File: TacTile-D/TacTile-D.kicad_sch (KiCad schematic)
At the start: 12 parts, among them J18 Conn_01x04, J18 Conn_01x06, J19 Conn_01x05, J19 Conn_01x06, J20 Conn_01x02, J20 Conn_01x06, J21 Conn_01x02, J21 Conn_01x06, U12 74HC595, U13 74HC590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

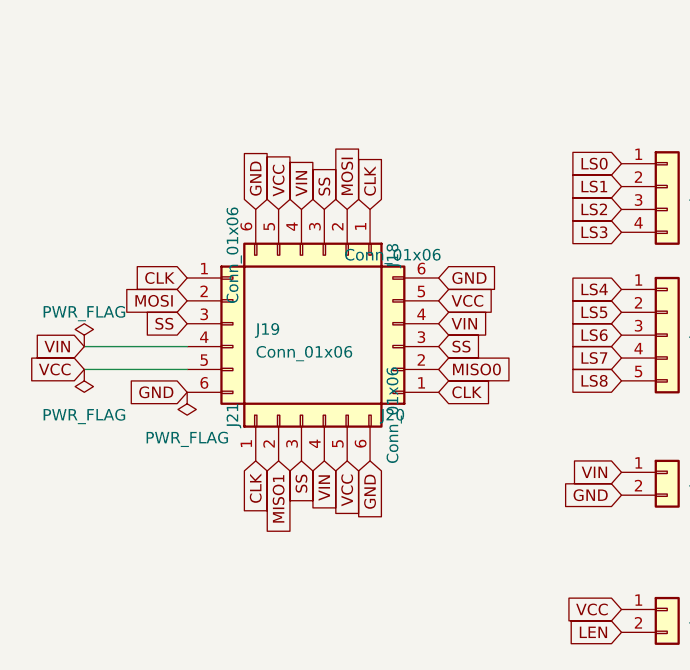
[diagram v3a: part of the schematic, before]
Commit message: Enlarged connectors on board D to 2.54mm pitch
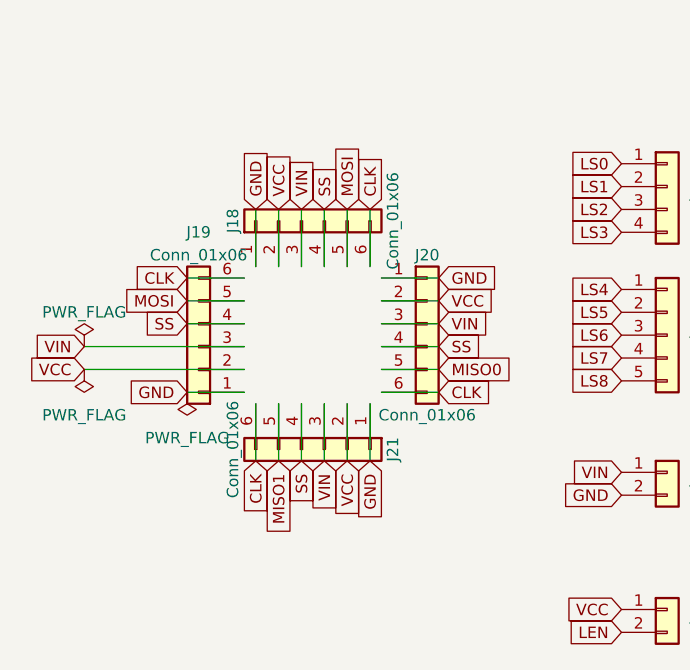
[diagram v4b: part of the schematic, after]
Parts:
- J18, J19: footprint Connector_PinHeader_2.00mm:PinHeader_1x06_P2.00mm_Horizontal -> Connector_PinSocket_2.54mm:PinSocket_1x06_P2.54mm_Horizontal
- J18: footprint Connector_PinSocket_1.27mm:PinSocket_1x04_P1.27mm_Vertical -> Connector_PinSocket_2.54mm:PinSocket_1x04_P2.54mm_Vertical
- J19: footprint Connector_PinSocket_1.27mm:PinSocket_1x05_P1.27mm_Vertical -> Connector_PinSocket_2.54mm:PinSocket_1x05_P2.54mm_Vertical
- J20, J21: footprint Connector_PinSocket_2.00mm:PinSocket_1x06_P2.00mm_Horizontal -> Connector_PinHeader_2.54mm:PinHeader_1x06_P2.54mm_Horizontal
- J20, J21: footprint Connector_PinSocket_1.27mm:PinSocket_1x02_P1.27mm_Vertical -> Connector_PinSocket_2.54mm:PinSocket_1x02_P2.54mm_Vertical
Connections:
- net CLK: now also J18.6 (Pin_6), J19.6 (Pin_6), J20.6 (Pin_6), J21.6 (Pin_6); no longer J18.1 (Pin_1), J19.1 (Pin_1), J20.1 (Pin_1), J21.1 (Pin_1)
- net GND: now also J18.1 (Pin_1), J19.1 (Pin_1), J20.1 (Pin_1), J21.1 (Pin_1); no longer J18.6 (Pin_6), J19.6 (Pin_6), J20.6 (Pin_6), J21.6 (Pin_6)
- net MISO0: now also J20.5 (Pin_5); no longer J20.2 (Pin_2)
- net MISO1: now also J21.5 (Pin_5); no longer J21.2 (Pin_2)
- net MOSI: now also J18.5 (Pin_5), J19.5 (Pin_5); no longer J18.2 (Pin_2), J19.2 (Pin_2)
- net SS: now also J18.4 (Pin_4), J19.4 (Pin_4), J20.4 (Pin_4), J21.4 (Pin_4); no longer J18.3 (Pin_3), J19.3 (Pin_3), J20.3 (Pin_3), J21.3 (Pin_3)
- net VCC: now also J18.2 (Pin_2), J19.2 (Pin_2), J20.2 (Pin_2), J21.2 (Pin_2); no longer J18.5 (Pin_5), J19.5 (Pin_5), J20.5 (Pin_5), J21.5 (Pin_5)
- net VIN: now also J18.3 (Pin_3), J19.3 (Pin_3), J20.3 (Pin_3), J21.3 (Pin_3); no longer J18.4 (Pin_4), J19.4 (Pin_4), J20.4 (Pin_4), J21.4 (Pin_4)
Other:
- moved on the sheet: J18, J19, J20, J21
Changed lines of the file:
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@@
+    (stroke (width 0) (type default))
+  )
+  (wire (pts (xy 46.99 21.59) (xy 46.99 27.94))
+    (stroke (width 0) (type default))
+  )
+  (wire (pts (xy 49.53 43.18) (xy 49.53 49.53))
     (stroke (width 0) (type default))
   )
@@
     (stroke (width 0) (type default))
   )
+  (wire (pts (xy 41.91 43.18) (xy 41.91 49.53))
+    (stroke (width 0) (type default))
+  )
+  (wire (pts (xy 53.34 39.37) (xy 59.69 39.37))
+    (stroke (width 0) (type default))
+  )
+  (wire (pts (xy 39.37 21.59) (xy 39.37 27.94))
+    (stroke (width 0) (type default))
+  )
   (wire (pts (xy 59.69 83.82) (xy 44.45 83.82))
     (stroke (width 0) (type default))
@@
     (stroke (width 0) (type default))
   )
+  (wire (pts (xy 44.45 21.59) (xy 44.45 27.94))
+    (stroke (width 0) (type default))
+  )
   (wire (pts (xy 129.54 128.27) (xy 129.54 91.44))
     (stroke (width 0) (type default))
   )
+  (wire (pts (xy 31.75 34.29) (xy 38.1 34.29))
+    (stroke (width 0) (type default))
+  )
   (wire (pts (xy 123.19 88.9) (xy 129.54 88.9))
     (stroke (width 0) (type default))
   )
+  (wire (pts (xy 53.34 34.29) (xy 59.69 34.29))
+    (stroke (width 0) (type default))
+  )
+  (wire (pts (xy 31.75 41.91) (xy 38.1 41.91))
+    (stroke (width 0) (type default))
+  )
   (wire (pts (xy 67.31 91.44) (xy 59.69 91.44))
     (stroke (width 0) (type default))
@@
     (stroke (width 0) (type default))
   )
+  (wire (pts (xy 31.75 31.75) (xy 38.1 31.75))
+    (stroke (width 0) (type default))
+  )
   (wire (pts (xy 67.31 96.52) (xy 67.31 95.25))
     (stroke (width 0) (type default))
@@
     (stroke (width 0) (type default))
   )
+  (wire (pts (xy 31.75 29.21) (xy 38.1 29.21))
+    (stroke (width 0) (type default))
+  )
+  (wire (pts (xy 20.32 39.37) (xy 38.1 39.37))
+    (stroke (width 0) (type default))
+  )
+  (wire (pts (xy 52.07 21.59) (xy 52.07 27.94))
+    (stroke (width 0) (type default))
+  )
   (wire (pts (xy 95.25 90.17) (xy 95.25 91.44))
     (stroke (width 0) (type default))
@@
     (stroke (width 0) (type default))
   )
-  (wire (pts (xy 20.32 39.37) (xy 31.75 39.37))
+  (wire (pts (xy 46.99 43.18) (xy 46.99 49.53))
+    (stroke (width 0) (type default))
+  )
+  (wire (pts (xy 41.91 21.59) (xy 41.91 27.94))
+    (stroke (width 0) (type default))
+  )
+  (wire (pts (xy 39.37 43.18) (xy 39.37 49.53))
     (stroke (width 0) (type default))
   )
@@
     (stroke (width 0) (type default))
   )
+  (wire (pts (xy 52.07 43.18) (xy 52.07 49.53))
+    (stroke (width 0) (type default))
+  )
+  (wire (pts (xy 44.45 43.18) (xy 44.45 49.53))
+    (stroke (width 0) (type default))
+  )
   (wire (pts (xy 59.69 91.44) (xy 59.69 83.82))
     (stroke (width 0) (type default))
   )
-  (wire (pts (xy 20.32 36.83) (xy 31.75 36.83))
+  (wire (pts (xy 53.34 31.75) (xy 59.69 31.75))
+    (stroke (width 0) (type default))
+  )
+  (wire (pts (xy 49.53 21.59) (xy 49.53 27.94))
+    (stroke (width 0) (type default))
+  )
+  (wire (pts (xy 53.34 41.91) (xy 59.69 41.91))
+    (stroke (width 0) (type default))
+  )
+  (wire (pts (xy 53.34 29.21) (xy 59.69 29.21))
+    (stroke (width 0) (type default))
+  )
+  (wire (pts (xy 53.34 36.83) (xy 59.69 36.83))
+    (stroke (width 0) (type default))
+  )
+  (wire (pts (xy 20.32 36.83) (xy 38.1 36.83))
     (stroke (width 0) (type default))
   )
@@
       (effects (font (size 1.27 1.27)) (justify left))
     )
-    (property "Footprint" "Connector_PinSocket_1.27mm:PinSocket_1x05_P1.27mm_Vertical" (at 85.09 35.56 0)
+    (property "Footprint" "Connector_PinSocket_2.54mm:PinSocket_1x05_P2.54mm_Vertical" (at 85.09 35.56 0)
       (effects (font (size 1.27 1.27)) hide)
     )
@@
     )
   )
-  (symbol (lib_id "Connector_Generic:Conn_01x06") (at 46.99 26.67 270) (unit 1)
+  (symbol (lib_id "Connector_Generic:Conn_01x06") (at 44.45 22.86 90) (unit 1)
     (in_bom yes) (on_board yes) (dnp no)
-    (property "Reference" "J18" (at 54.61 26.67 0)
-      (effects (font (size 1.27 1.27)))
-    )
-    (property "Value" "Conn_01x06" (at 36.83 26.67 0)
-      (effects (font (size 1.27 1.27)))
-    )
-    (property "Footprint" "Connector_PinHeader_2.00mm:PinHeader_1x06_P2.00mm_Horizontal" (at 46.99 26.67 0)
-      (effects (font (size 1.27 1.27)) hide)
-    )
-    (property "Datasheet" "~" (at 46.99 26.67 0)
+    (property "Reference" "J18" (at 36.83 22.86 0)
+      (effects (font (size 1.27 1.27)))
+    )
+    (property "Value" "Conn_01x06" (at 54.61 22.86 0)
+      (effects (font (size 1.27 1.27)))
+    )
+    (property "Footprint" "Connector_PinSocket_2.54mm:PinSocket_1x06_P2.54mm_Horizontal" (at 44.45 22.86 0)
+      (effects (font (size 1.27 1.27)) hide)
+    )
+    (property "Datasheet" "~" (at 44.45 22.86 0)
       (effects (font (size 1.27 1.27)) hide)
     )
@@
     )
   )
-  (symbol (lib_id "Connector_Generic:Conn_01x06") (at 54.61 36.83 180) (unit 1)
+  (symbol (lib_id "Connector_Generic:Conn_01x06") (at 58.42 34.29 0) (unit 1)
     (in_bom yes) (on_board yes) (dnp no)
-    (property "Reference" "J20" (at 54.61 44.45 0)
-      (effects (font (size 1.27 1.27)))
-    )
-    (property "Value" "Conn_01x06" (at 54.61 26.67 0)
-      (effects (font (size 1.27 1.27)))
-    )
-    (property "Footprint" "Connector_PinSocket_2.00mm:PinSocket_1x06_P2.00mm_Horizontal" (at 54.61 36.83 0)
-      (effects (font (size 1.27 1.27)) hide)
-    )
-    (property "Datasheet" "~" (at 54.61 36.83 0)
+    (property "Reference" "J20" (at 58.42 26.67 0)
+      (effects (font (size 1.27 1.27)))
+    )
+    (property "Value" "Conn_01x06" (at 58.42 44.45 0)
+      (effects (font (size 1.27 1.27)))
+    )
+    (property "Footprint" "Connector_PinHeader_2.54mm:PinHeader_1x06_P2.54mm_Horizontal" (at 58.42 34.29 0)
+      (effects (font (size 1.27 1.27)) hide)
+    )
+    (property "Datasheet" "~" (at 58.42 34.29 0)
       (effects (font (size 1.27 1.27)) hide)
     )
@@
       (effects (font (size 1.27 1.27)) (justify left))
     )
-    (property "Footprint" "Connector_PinSocket_1.27mm:PinSocket_1x02_P1.27mm_Vertical" (at 85.09 66.04 0)
+    (property "Footprint" "Connector_PinSocket_2.54mm:PinSocket_1x02_P2.54mm_Vertical" (at 85.09 66.04 0)
       (effects (font (size 1.27 1.27)) hide)
     )
@@
       (effects (font (size 1.27 1.27)) (justify left))
     )
-    (property "Footprint" "Connector_PinSocket_1.27mm:PinSocket_1x04_P1.27mm_Vertical" (at 85.09 19.05 0)
+    (property "Footprint" "Connector_PinSocket_2.54mm:PinSocket_1x04_P2.54mm_Vertical" (at 85.09 19.05 0)
       (effects (font (size 1.27 1.27)) hide)
     )
@@
       (effects (font (size 1.27 1.27)) (justify left))
     )
-    (property "Footprint" "Connector_PinSocket_1.27mm:PinSocket_1x02_P1.27mm_Vertical" (at 85.09 50.8 0)
+    (property "Footprint" "Connector_PinSocket_2.54mm:PinSocket_1x02_P2.54mm_Vertical" (at 85.09 50.8 0)
       (effects (font (size 1.27 1.27)) hide)
     )
@@
     )
   )
-  (symbol (lib_id "Connector_Generic:Conn_01x06") (at 36.83 34.29 0) (unit 1)
-    (in_bom yes) (on_board yes) (dnp no) (fields_autoplaced)
-    (property "Reference" "J19" (at 39.37 34.925 0)
-      (effects (font (size 1.27 1.27)) (justify left))
-    )
-    (property "Value" "Conn_01x06" (at 39.37 37.465 0)
-      (effects (font (size 1.27 1.27)) (justify left))
-    )
-    (property "Footprint" "Connector_PinHeader_2.00mm:PinHeader_1x06_P2.00mm_Horizontal" (at 36.83 34.29 0)
-      (effects (font (size 1.27 1.27)) hide)
-    )
-    (property "Datasheet" "~" (at 36.83 34.29 0)
+  (symbol (lib_id "Connector_Generic:Conn_01x06") (at 33.02 36.83 180) (unit 1)
+    (in_bom yes) (on_board yes) (dnp no) (fields_autoplaced)
+    (property "Reference" "J19" (at 33.02 24.13 0)
+      (effects (font (size 1.27 1.27)))
+    )
+    (property "Value" "Conn_01x06" (at 33.02 26.67 0)
+      (effects (font (size 1.27 1.27)))
+    )
+    (property "Footprint" "Connector_PinSocket_2.54mm:PinSocket_1x06_P2.54mm_Horizontal" (at 33.02 36.83 0)
+      (effects (font (size 1.27 1.27)) hide)
+    )
+    (property "Datasheet" "~" (at 33.02 36.83 0)
       (effects (font (size 1.27 1.27)) hide)
     )
@@
     )
   )
-  (symbol (lib_id "Connector_Generic:Conn_01x06") (at 44.45 44.45 90) (unit 1)
+  (symbol (lib_id "Connector_Generic:Conn_01x06") (at 46.99 48.26 270) (unit 1)
     (in_bom yes) (on_board yes) (dnp no)
-    (property "Reference" "J21" (at 36.83 44.45 0)
-      (effects (font (size 1.27 1.27)))
-    )
-    (property "Value" "Conn_01x06" (at 54.61 44.45 0)
-      (effects (font (size 1.27 1.27)))
-    )
-    (property "Footprint" "Connector_PinSocket_2.00mm:PinSocket_1x06_P2.00mm_Horizontal" (at 44.45 44.45 0)
-      (effects (font (size 1.27 1.27)) hide)
-    )
-    (property "Datasheet" "~" (at 44.45 44.45 0)
-      (effects (font (size 1.27 1.27)) hide)
-    )
+    (property "Reference" "J21" (at 54.61 48.26 0)
+      (effects (font (size 1.27 1.27)))
+    )
+    (property "Value" "Conn_01x06" (at 36.83 48.26 0)
+      (effects (font (size 1.27 1.27)))
+    )
+    (property "Footprint" "Connector_PinHeader_2.54mm:PinHeader_1x06_P2.54mm_Horizontal" (at 46.99 48.26 0)
+      (effects (font (size 1.27 1.27)) hide)
+    )
+    (property "Datasheet" "~" (at 46.99 48.26 0)
+      (effects (font (size 1.27 1.27)) hide)
+    )

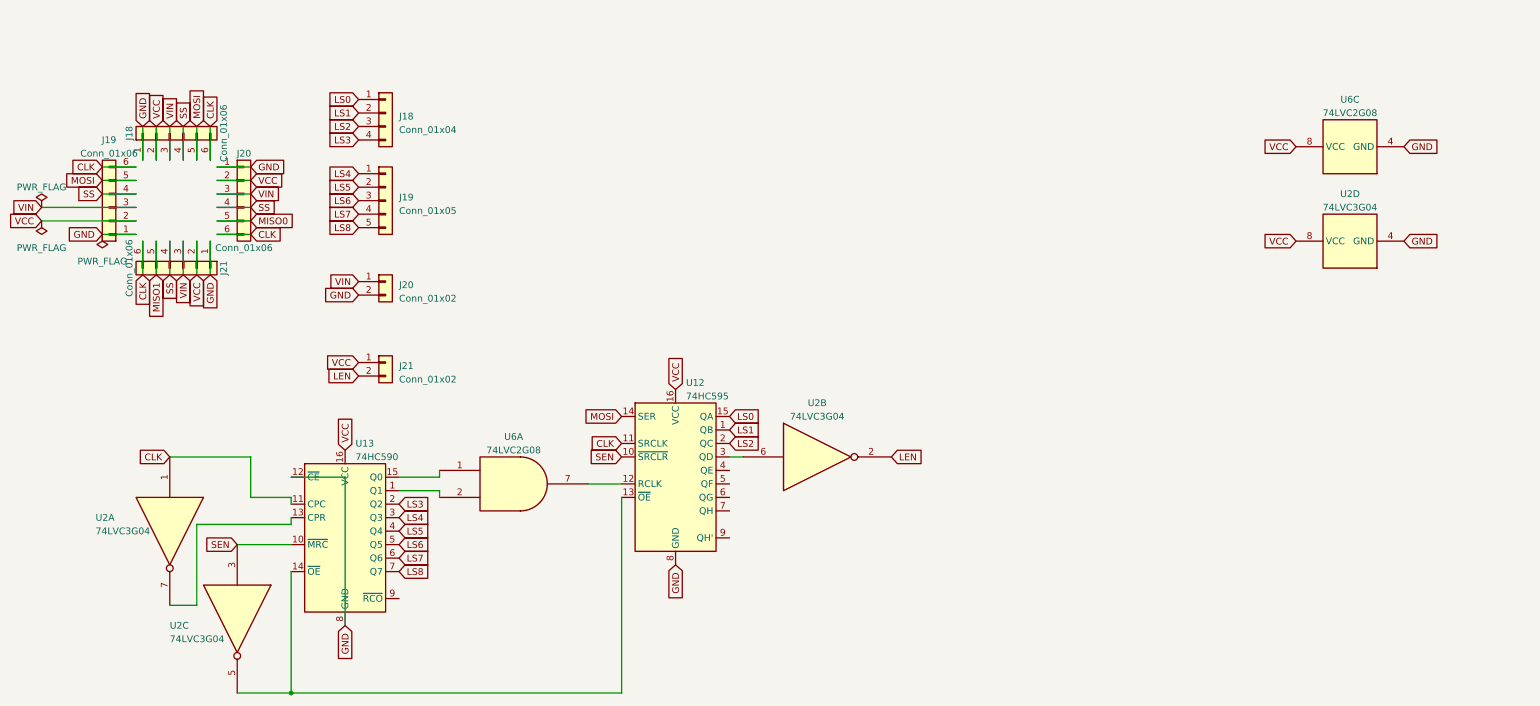
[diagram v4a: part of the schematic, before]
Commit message: Updated D schematic to reflect available ICs
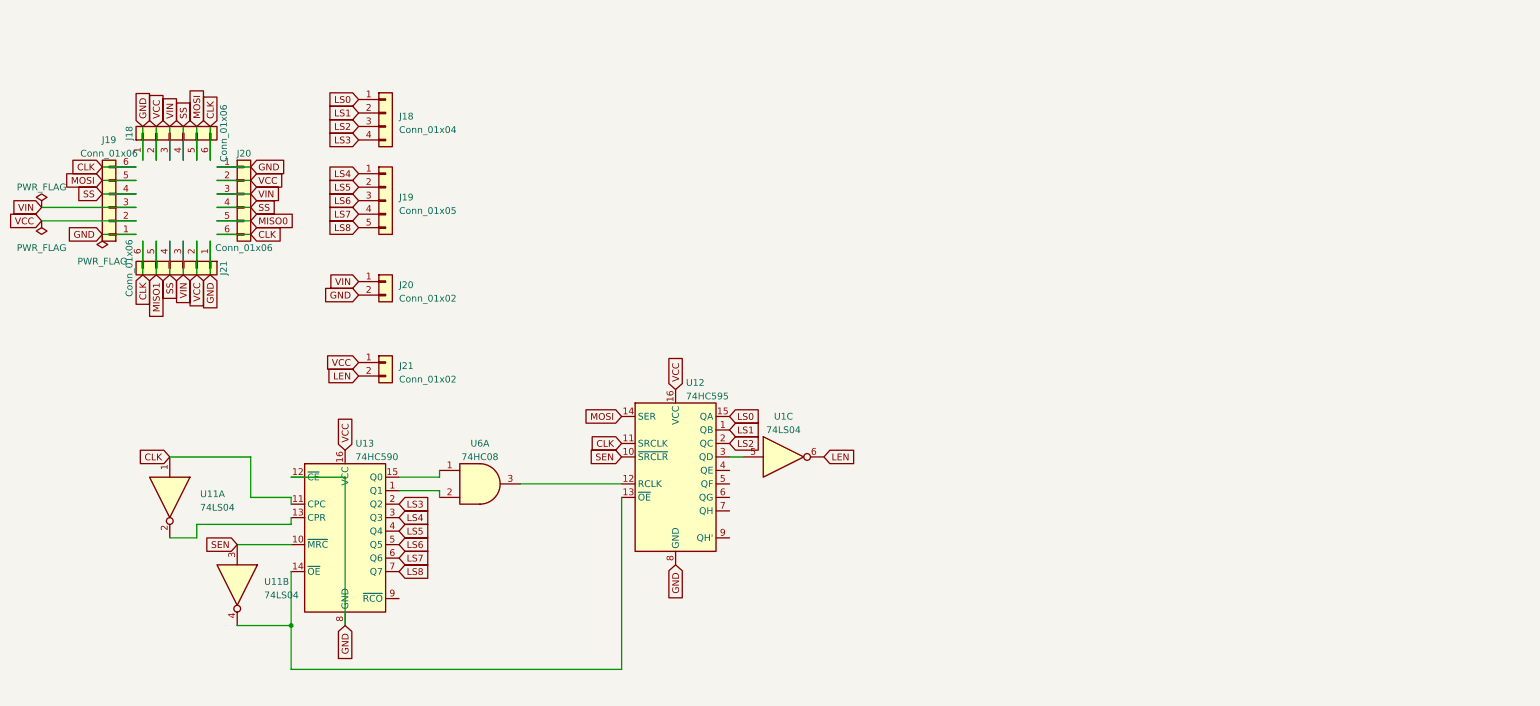
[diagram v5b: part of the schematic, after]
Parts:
- removed U2: 74LVC3G04, Package_DIP:DIP-8_W7.62mm, symbol 74xGxx:74LVC3G04
- removed U6: 74LVC2G08, Package_DIP:DIP-8_W7.62mm, symbol 74xGxx:74LVC2G08
- added U1, U11: 74LS04, Package_DIP:DIP-14_W7.62mm, symbol 74xx:74LS04
- added U6: 74HC08, symbol TacTile:74HC08
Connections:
- net CLK: now also U11.1
- net LEN: now also U1.6
- net SEN: now also U11.3
- net at U12.12 (RCLK): now also U6.3
- net at U12.13 (~{OE}), U13.14 (~{OE}): now also U11.4
- net at U12.3 (QD): now also U1.5
- net at U13.15 (Q0): now also U6.1
- net at U13.1 (Q1): now also U6.2
- net at U13.13 (CPR): now also U11.2

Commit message: Checked new board D spacing requirements
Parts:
- U6: footprint (none) -> Package_DIP:DIP-14_W7.62mm
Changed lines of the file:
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@@
       (effects (font (size 1.27 1.27)))
     )
-    (property "Footprint" "" (at 102.87 88.9 0)
+    (property "Footprint" "Package_DIP:DIP-14_W7.62mm" (at 102.87 88.9 0)
       (effects (font (size 1.27 1.27)) hide)
     )

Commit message: Updated more fabrication files and D board selecting wrong coil
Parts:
- removed U1: 74LS04, Package_DIP:DIP-14_W7.62mm, symbol 74xx:74LS04
- added U2: 4011, symbol 4xxx:4011
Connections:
- net LEN: now also U2.11
- net at U12.12 (RCLK), U6.3: now also U2.12
- net at U12.3 (QD): now also U2.13
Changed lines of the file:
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@@
   (junction (at 67.31 115.57) (diameter 0) (color 0 0 0 0)
   )
+  (junction (at 112.395 88.9) (diameter 0) (color 0 0 0 0)
+  )
   (wire (pts (xy 67.31 123.825) (xy 129.54 123.825))
     (stroke (width 0) (type default))
@@
     (stroke (width 0) (type default))
   )
+  (wire (pts (xy 112.395 88.9) (xy 112.395 61.595))
+    (stroke (width 0) (type default))
+  )
   (wire (pts (xy 49.53 96.52) (xy 67.31 96.52))
     (stroke (width 0) (type default))
@@
     (stroke (width 0) (type default))
   )
-  (wire (pts (xy 149.86 83.82) (xy 152.4 83.82))
-    (stroke (width 0) (type default))
-  )
   (wire (pts (xy 31.75 31.75) (xy 38.1 31.75))
     (stroke (width 0) (type default))
   )
+  (wire (pts (xy 160.02 83.82) (xy 160.02 66.675))
+    (stroke (width 0) (type default))
+  )
   (wire (pts (xy 67.31 96.52) (xy 67.31 95.25))
     (stroke (width 0) (type default))
@@
     (stroke (width 0) (type default))
   )
+  (wire (pts (xy 112.395 61.595) (xy 160.02 61.595))
+    (stroke (width 0) (type default))
+  )
   (wire (pts (xy 52.07 21.59) (xy 52.07 27.94))
     (stroke (width 0) (type default))
   )
+  (wire (pts (xy 149.86 83.82) (xy 160.02 83.82))
+    (stroke (width 0) (type default))
+  )
   (wire (pts (xy 46.99 43.18) (xy 46.99 49.53))
     (stroke (width 0) (type default))
@@
     (stroke (width 0) (type default))
   )
-  (wire (pts (xy 110.49 88.9) (xy 129.54 88.9))
+  (wire (pts (xy 110.49 88.9) (xy 112.395 88.9))
     (stroke (width 0) (type default))
   )
@@
     (stroke (width 0) (type default))
   )
+  (wire (pts (xy 112.395 88.9) (xy 129.54 88.9))
+    (stroke (width 0) (type default))
+  )
   (wire (pts (xy 87.63 90.17) (xy 95.25 90.17))
     (stroke (width 0) (type default))
@@
     )
   )
-  (global_label "LEN" (shape input) (at 167.64 83.82 0) (fields_autoplaced)
-    (effects (font (size 1.27 1.27)) (justify left))
-    (property "Intersheetrefs" "${INTERSHEET_REFS}" (at 174.0534 83.82 0)
+  (global_label "LEN" (shape input) (at 175.26 64.135 0) (fields_autoplaced)
+    (effects (font (size 1.27 1.27)) (justify left))
+    (property "Intersheetrefs" "${INTERSHEET_REFS}" (at 181.6734 64.135 0)
       (effects (font (size 1.27 1.27)) (justify left) hide)
     )
@@
     )
   )
-  (symbol (lib_id "74xx:74LS04") (at 160.02 83.82 0) (unit 3)
+  (symbol (lib_id "4xxx:4011") (at 167.64 64.135 0) (unit 4)
     (in_bom yes) (on_board yes) (dnp no) (fields_autoplaced)
-    (property "Reference" "U1" (at 160.02 76.2 0)
-      (effects (font (size 1.27 1.27)))
-    )
-    (property "Value" "74LS04" (at 160.02 78.74 0)
-      (effects (font (size 1.27 1.27)))
-    )
-    (property "Footprint" "Package_DIP:DIP-14_W7.62mm" (at 160.02 83.82 0)
-      (effects (font (size 1.27 1.27)) hide)
-    )
-    (property "Datasheet" "http://www.ti.com/lit/gpn/sn74LS04" (at 160.02 83.82 0)
+    (property "Reference" "U2" (at 167.6317 55.88 0)
+      (effects (font (size 1.27 1.27)))
+    )
+    (property "Value" "4011" (at 167.6317 58.42 0)
+      (effects (font (size 1.27 1.27)))
+    )
+    (property "Footprint" "" (at 167.64 64.135 0)
+      (effects (font (size 1.27 1.27)) hide)
+    )
+    (property "Datasheet" "http://www.intersil.com/content/dam/Intersil/documents/cd40/cd4011bms-12bms-23bms.pdf" (at 167.64 64.135 0)
       (effects (font (size 1.27 1.27)) hide)
     )
@@
     (pin "5")
     (pin "6")
+    (pin "10")
     (pin "8")
     (pin "9")
-    (pin "10")
     (pin "11")
     (pin "12")
@@
     (instances
       (project "TacTile-D"
-        (path "/99b9cae1-6ece-4124-abcb-60ec0df49dce/db500e62-b4b7-46ca-b547-61dad2cea336"
-          (reference "U1") (unit 3)
-        )
-        (path "/99b9cae1-6ece-4124-abcb-60ec0df49dce"
-          (reference "U1") (unit 3)
-        )
-      )
+        (path "/99b9cae1-6ece-4124-abcb-60ec0df49dce"
+          (reference "U2") (unit 4)
+        )
+      )
